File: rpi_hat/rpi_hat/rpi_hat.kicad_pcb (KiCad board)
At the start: 2 copper layers, 38.9 x 52.3 mm, 17 parts, among them J1 Raspberry_Pi_2_3, J2 Screw_Terminal_01x02, J3 Screw_Terminal_01x02, J4 Screw_Terminal_01x02, J5 Screw_Terminal_01x02, Q1 2SC1815, Q2 2N7000, U1 L7805

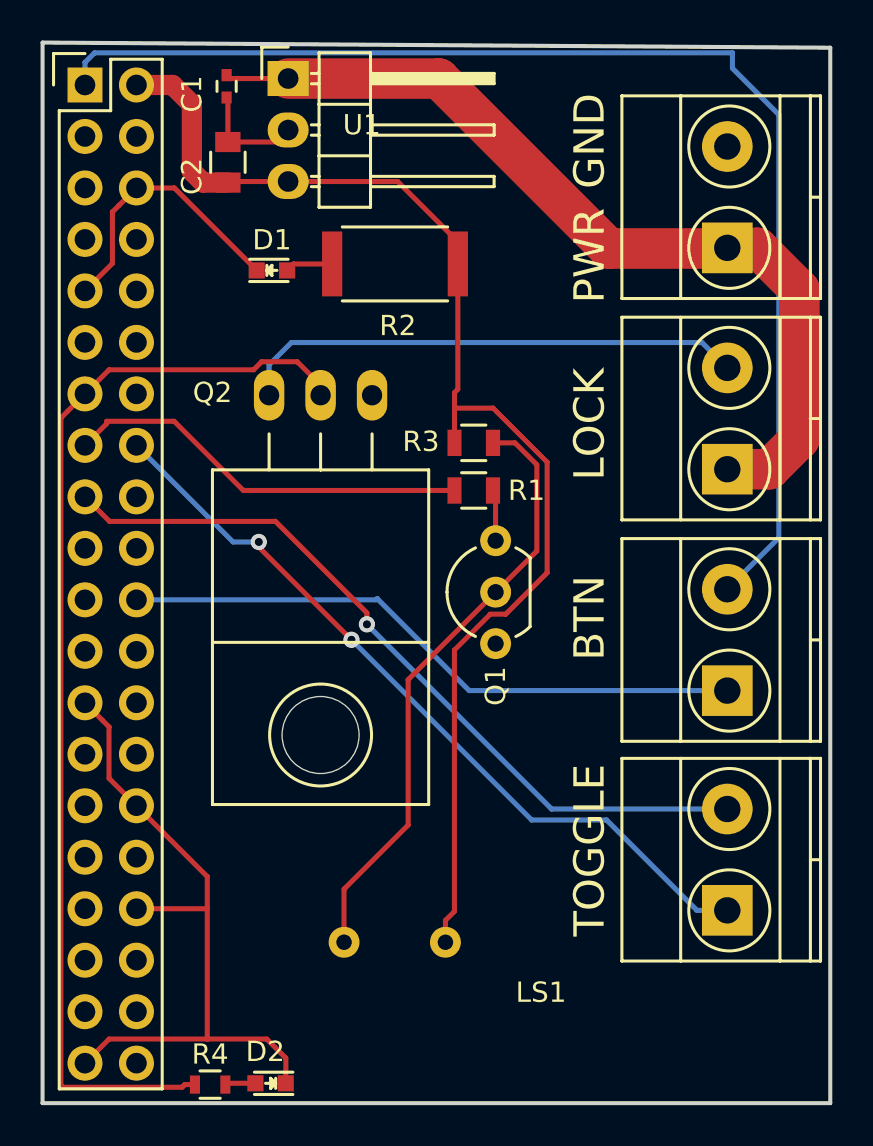
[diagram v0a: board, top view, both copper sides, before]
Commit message: Fix pushbutton switch circuit so it doesn't rely on the Pi working
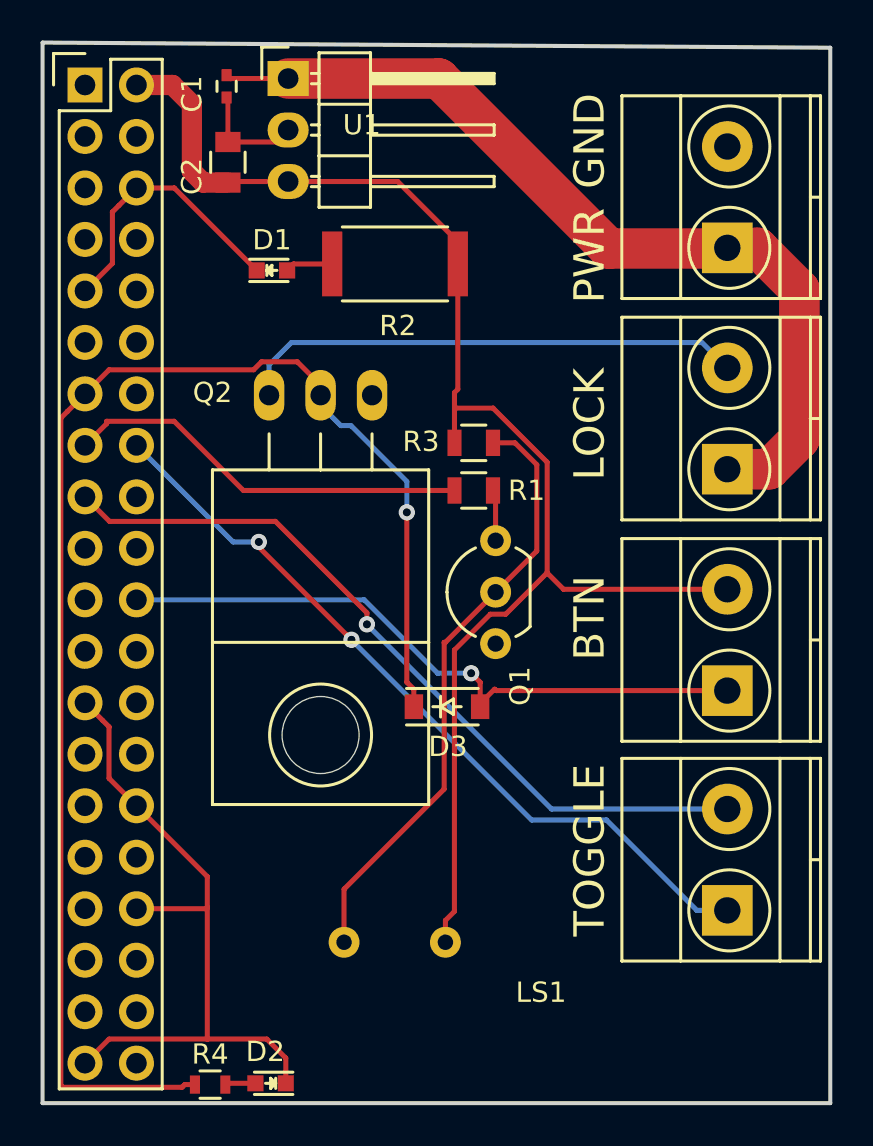
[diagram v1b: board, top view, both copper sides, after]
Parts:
- added D3: D, Diodes_SMD:SOD-123, F.Cu at (146.2, 91.4)
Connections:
- J1 pad 1: SwitchPWR -> (no net)
- J3 pad 2: SwitchPWR -> Vcc
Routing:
- net SwitchPWR: track 61.7 -> 0.00 mm
- net Lock: track 54.6 -> 72.1 mm, vias 0 -> 1
- net Vcc: track 63.2 -> 72.4 mm
- net Switch: track 31.1 -> 32.5 mm, vias 0 -> 1

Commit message: Add protection diode
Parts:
- added D4: D_Schottky, Diodes_SMD:SOD-123, F.Cu at (146.9, 73.3)
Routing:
- net Vin: track 45.8 -> 53.3 mm
- net Net-(D4-Pad2): track 25.1 -> 26.6 mm, vias 0 -> 1
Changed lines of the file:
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@@
     (thickness 1.6)
     (drawings 9)
-    (tracks 137)
+    (tracks 144)
     (zones 0)
-    (modules 18)
+    (modules 19)
     (nets 14)
   )
@@
   (net 9 TogglePWR)
   (net 10 Switch)
-  (net 11 "Net-(J5-Pad2)")
-  (net 12 "Net-(LS1-Pad2)")
-  (net 13 "Net-(Q1-Pad3)")
+  (net 11 "Net-(LS1-Pad2)")
+  (net 12 "Net-(Q1-Pad3)")
+  (net 13 "Net-(D4-Pad2)")
   (net_class Default "This is the default net class."
     (clearance 0.2)
@@
     (add_net "Net-(D1-Pad2)")
     (add_net "Net-(D2-Pad2)")
-    (add_net "Net-(J5-Pad2)")
+    (add_net "Net-(D4-Pad2)")
     (add_net "Net-(LS1-Pad2)")
     (add_net "Net-(Q1-Pad3)")
@@
       (net 1 Vin))
     (pad 2 thru_hole circle (at 5 0 90) (size 2.5 2.5) (drill 1.3) (layers *.Cu *.Mask F.SilkS)
-      (net 11 "Net-(J5-Pad2)"))
+      (net 13 "Net-(D4-Pad2)"))
     (model Terminal_Blocks.3dshapes/TerminalBlock_Pheonix_MKDS1.5-2pol.wrl
       (offset (xyz 2.499359962463379 0 0))
@@
       (net 3 Vcc))
     (pad 2 thru_hole circle (at 2.5 0 180) (size 1.524 1.524) (drill 0.762) (layers *.Cu *.Mask)
-      (net 12 "Net-(LS1-Pad2)"))
+      (net 11 "Net-(LS1-Pad2)"))
   )
   (module TO_SOT_Packages_THT:TO-92_Inline_Wide (layer F.Cu)
@@
     (fp_line (start 6.1 1.95) (end 6.1 -2.65) (layer F.CrtYd) (width 0.05))
     (pad 2 thru_hole circle (at 2.54 0 180) (size 1.524 1.524) (drill 0.8) (layers *.Cu *.Mask F.SilkS)
-      (net 12 "Net-(LS1-Pad2)"))
+      (net 11 "Net-(LS1-Pad2)"))
     (pad 3 thru_hole circle (at 5.08 0 180) (size 1.524 1.524) (drill 0.8) (layers *.Cu *.Mask F.SilkS)
-      (net 13 "Net-(Q1-Pad3)"))
+      (net 12 "Net-(Q1-Pad3)"))
     (pad 1 thru_hole circle (at 0 0 180) (size 1.524 1.524) (drill 0.8) (layers *.Cu *.Mask F.SilkS)
       (net 2 GND))
@@
       (net 2 GND))
     (pad 3 thru_hole oval (at 2.54 0 270) (size 2.49936 1.50114) (drill 1.00076) (layers *.Cu *.Mask F.SilkS)
-      (net 11 "Net-(J5-Pad2)"))
+      (net 13 "Net-(D4-Pad2)"))
     (pad "" np_thru_hole circle (at 0 -16.764 270) (size 3.79984 3.79984) (drill 3.79984) (layers *.Cu *.Mask F.SilkS))
     (model TO_SOT_Packages_THT.3dshapes/TO-220_Neutral123_Horizontal.wrl
@@
       (net 7 Alert))
     (pad 1 smd rect (at -0.95 0 180) (size 0.7 1.3) (layers F.Cu F.Paste F.Mask)
-      (net 13 "Net-(Q1-Pad3)"))
+      (net 12 "Net-(Q1-Pad3)"))
     (model Resistors_SMD.3dshapes/R_0805.wrl
       (at (xyz 0 0 0))
@@
       (net 3 Vcc))
     (pad 2 smd rect (at 0.95 0) (size 0.7 1.3) (layers F.Cu F.Paste F.Mask)
-      (net 12 "Net-(LS1-Pad2)"))
+      (net 11 "Net-(LS1-Pad2)"))
     (model Resistors_SMD.3dshapes/R_0805.wrl
       (at (xyz 0 0 0))
@@
       (net 10 Switch))
   )
+  (module Diodes_SMD:SOD-123 (layer F.Cu)
+    (at 146.8755 73.279 180)
+    (descr SOD-123)
+    (tags SOD-123)
+    (attr smd)
+    (fp_text reference D4 (at 0 -2 180) (layer F.SilkS)
+      (effects (font (size 1 1) (thickness 0.15)))
+    )
+    (fp_text value D_Schottky (at 0 2.1 180) (layer F.Fab)
+      (effects (font (size 1 1) (thickness 0.15)))
+    )
+    (fp_line (start 0.3175 0) (end 0.6985 0) (layer F.SilkS) (width 0.15))
+    (fp_line (start -0.6985 0) (end -0.3175 0) (layer F.SilkS) (width 0.15))
+    (fp_line (start -0.3175 0) (end 0.3175 -0.381) (layer F.SilkS) (width 0.15))
+    (fp_line (start 0.3175 -0.381) (end 0.3175 0.381) (layer F.SilkS) (width 0.15))
+    (fp_line (start 0.3175 0.381) (end -0.3175 0) (layer F.SilkS) (width 0.15))
+    (fp_line (start -0.3175 -0.508) (end -0.3175 0.508) (layer F.SilkS) (width 0.15))
+    (fp_line (start -2.25 -1.05) (end 2.25 -1.05) (layer F.CrtYd) (width 0.05))
+    (fp_line (start 2.25 -1.05) (end 2.25 1.05) (layer F.CrtYd) (width 0.05))
+    (fp_line (start 2.25 1.05) (end -2.25 1.05) (layer F.CrtYd) (width 0.05))
+    (fp_line (start -2.25 -1.05) (end -2.25 1.05) (layer F.CrtYd) (width 0.05))
+    (fp_line (start -2 0.9) (end 1.54 0.9) (layer F.SilkS) (width 0.15))
+    (fp_line (start -2 -0.9) (end 1.54 -0.9) (layer F.SilkS) (width 0.15))
+    (pad 1 smd rect (at -1.635 0 180) (size 0.91 1.22) (layers F.Cu F.Paste F.Mask)
+      (net 1 Vin))
+    (pad 2 smd rect (at 1.635 0 180) (size 0.91 1.22) (layers F.Cu F.Paste F.Mask)
+      (net 13 "Net-(D4-Pad2)"))
+  )
   (gr_line (start 165.1 58.928) (end 126.238 58.674) (layer Edge.Cuts) (width 0.2))
   (gr_line (start 165.1 110.998) (end 165.1 58.928) (layer Edge.Cuts) (width 0.2))
@@
   (segment (start 163.576 70.858) (end 163.576 78.232) (width 2) (layer F.Cu) (net 1))
   (segment (start 161.52 68.802) (end 163.576 70.858) (width 2) (layer F.Cu) (net 1))
+  (segment (start 153.6605 68.834) (end 154.178 68.834) (width 0.25) (layer F.Cu) (net 1))
+  (segment (start 149.2155 73.279) (end 153.6605 68.834) (width 0.25) (layer F.Cu) (net 1))
+  (segment (start 148.5105 73.279) (end 149.2155 73.279) (width 0.25) (layer F.Cu) (net 1))
   (segment (start 128.330501 109.026501) (end 129.519102 107.8379) (width 0.25) (layer F.Cu) (net 2) (status 10))
   (segment (start 138.238367 108.774367) (end 138.238367 110.020606) (width 0.25) (layer F.Cu) (net 2) (status 20))
@@
   (segment (start 147.3835 89.789) (end 145.726002 89.789) (width 0.25) (layer B.Cu) (net 10))
   (segment (start 145.726002 89.789) (end 142.103503 86.166501) (width 0.25) (layer B.Cu) (net 10))
-  (segment (start 138.513319 73.474001) (end 158.770001 73.474001) (width 0.25) (layer B.Cu) (net 11))
-  (segment (start 137.414 74.57332) (end 138.513319 73.474001) (width 0.25) (layer B.Cu) (net 11))
-  (segment (start 158.770001 73.474001) (end 160.02 74.724) (width 0.25) (layer B.Cu) (net 11) (status 20))
-  (segment (start 137.414 76.073) (end 137.414 74.57332) (width 0.25) (layer B.Cu) (net 11) (status 10))
-  (segment (start 150.622 83.7565) (end 148.59 85.7885) (width 0.25) (layer F.Cu) (net 12) (status 20))
-  (segment (start 150.622 83.7565) (end 150.622 79.502) (width 0.25) (layer F.Cu) (net 12))
-  (segment (start 149.5425 78.4225) (end 148.4605 78.4225) (width 0.25) (layer F.Cu) (net 12) (status 20))
-  (segment (start 150.622 79.502) (end 149.5425 78.4225) (width 0.25) (layer F.Cu) (net 12))
-  (segment (start 146.1135 88.265) (end 148.59 85.7885) (width 0.25) (layer F.Cu) (net 12))
-  (segment (start 146.05 88.265) (end 146.1135 88.265) (width 0.25) (layer F.Cu) (net 12))
-  (segment (start 146.05 95.504) (end 146.05 88.265) (width 0.25) (layer F.Cu) (net 12))
-  (segment (start 141.1135 103.0605) (end 141.1135 100.4405) (width 0.25) (layer F.Cu) (net 12))
-  (segment (start 141.1135 100.4405) (end 146.05 95.504) (width 0.25) (layer F.Cu) (net 12))
-  (segment (start 148.59 80.9015) (end 148.4605 80.772) (width 0.25) (layer F.Cu) (net 13) (status 30))
-  (segment (start 148.59 83.2485) (end 148.59 80.9015) (width 0.25) (layer F.Cu) (net 13) (status 30))
+  (segment (start 137.414 74.57332) (end 138.513319 73.474001) (width 0.25) (layer B.Cu) (net 13))
+  (segment (start 158.770001 73.474001) (end 160.02 74.724) (width 0.25) (layer B.Cu) (net 13) (status 20))
+  (segment (start 137.414 76.073) (end 137.414 74.57332) (width 0.25) (layer B.Cu) (net 13) (status 10))
+  (segment (start 150.622 83.7565) (end 148.59 85.7885) (width 0.25) (layer F.Cu) (net 11) (status 20))
+  (segment (start 150.622 83.7565) (end 150.622 79.502) (width 0.25) (layer F.Cu) (net 11))
+  (segment (start 149.5425 78.4225) (end 148.4605 78.4225) (width 0.25) (layer F.Cu) (net 11) (status 20))
+  (segment (start 150.622 79.502) (end 149.5425 78.4225) (width 0.25) (layer F.Cu) (net 11))
+  (segment (start 146.1135 88.265) (end 148.59 85.7885) (width 0.25) (layer F.Cu) (net 11))
+  (segment (start 146.05 88.265) (end 146.1135 88.265) (width 0.25) (layer F.Cu) (net 11))
+  (segment (start 146.05 95.504) (end 146.05 88.265) (width 0.25) (layer F.Cu) (net 11))
+  (segment (start 141.1135 103.0605) (end 141.1135 100.4405) (width 0.25) (layer F.Cu) (net 11))
+  (segment (start 141.1135 100.4405) (end 146.05 95.504) (width 0.25) (layer F.Cu) (net 11))
+  (segment (start 148.59 80.9015) (end 148.4605 80.772) (width 0.25) (layer F.Cu) (net 12) (status 30))
+  (segment (start 148.59 83.2485) (end 148.59 80.9015) (width 0.25) (layer F.Cu) (net 12) (status 30))
+  (via (at 143.8275 73.474001) (size 0.8) (drill 0.4) (layers F.Cu B.Cu) (net 13))
+  (segment (start 144.022501 73.279) (end 143.8275 73.474001) (width 0.25) (layer F.Cu) (net 13))
+  (segment (start 145.2405 73.279) (end 144.022501 73.279) (width 0.25) (layer F.Cu) (net 13))
+  (segment (start 138.513319 73.474001) (end 143.8275 73.474001) (width 0.25) (layer B.Cu) (net 13))
+  (segment (start 143.8275 73.474001) (end 158.770001 73.474001) (width 0.25) (layer B.Cu) (net 13))
   (zone (net 2) (net_name GND) (layer B.Cu) (hatch edge 0.508)
     (connect_pads (clearance 0.508))
